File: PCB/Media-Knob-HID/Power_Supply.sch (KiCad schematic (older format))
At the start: 19 parts

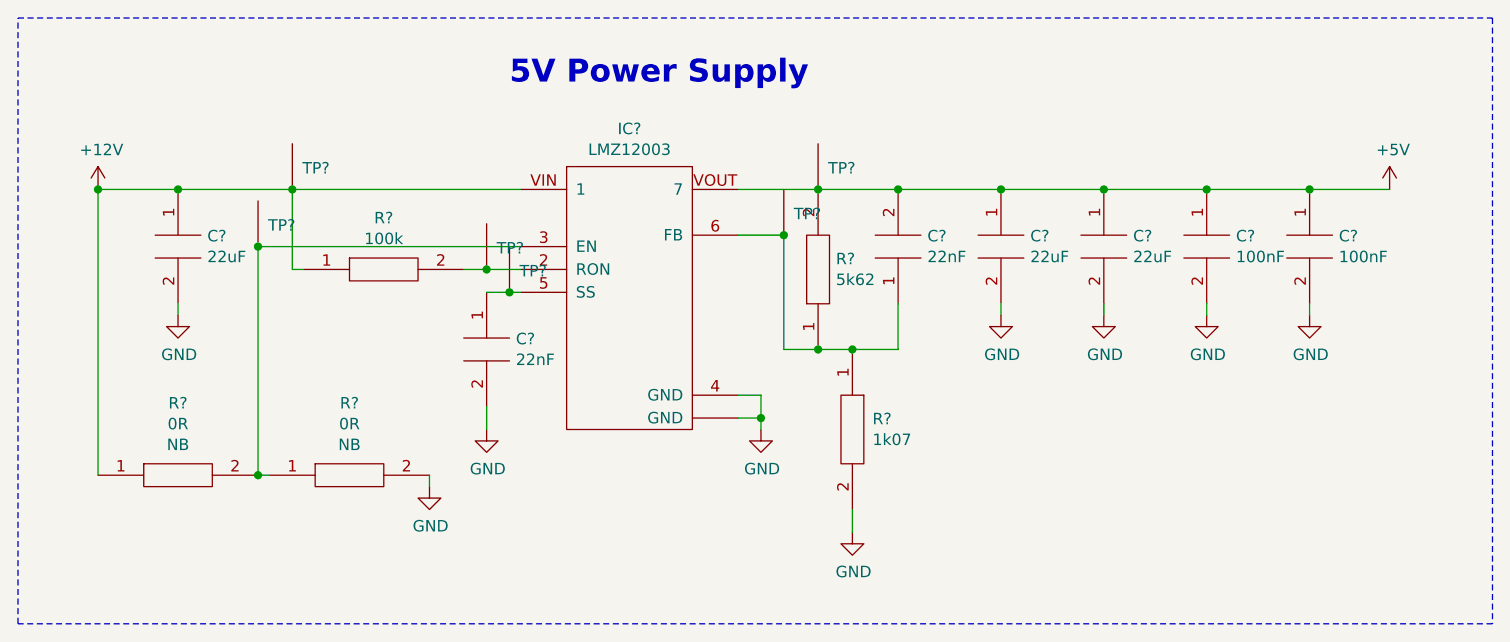
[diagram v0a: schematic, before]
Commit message: Port Switch für USB eingefügt
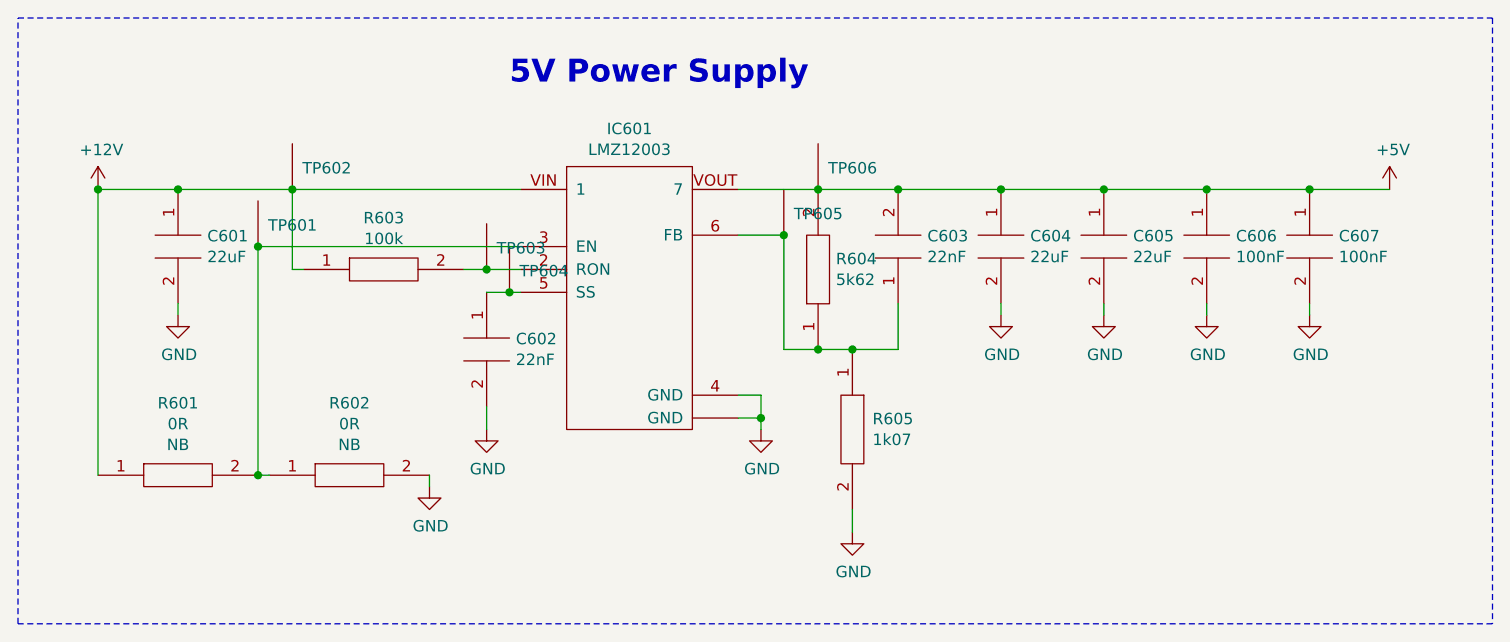
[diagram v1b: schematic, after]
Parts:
- gave numbers to parts that had none: 19
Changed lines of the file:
@@
 $Descr A3 16535 11693
 encoding utf-8
-Sheet 6 7
+Sheet 6 8
 Title "Media-Knob_HID"
 Date "2020-12-13"
@@
 $EndDescr
 $Comp
-L Artikel:LMZ12003 IC?
+L Artikel:LMZ12003 IC601
 U 1 1 607EAA9F
 P 3950 1900
-F 0 "IC?" H 3925 2615 50  0000 C CNN
+F 0 "IC601" H 3925 2615 50  0000 C CNN
 F 1 "LMZ12003" H 3925 2524 50  0000 C CNN
 F 2 "" H 3850 1850 50  0001 C CNN
@@
 $EndComp
 $Comp
-L power:GND #PWR?
+L power:GND #PWR0605
 U 1 1 607EB63F
 P 4500 2500
-F 0 "#PWR?" H 4500 2250 50  0001 C CNN
+F 0 "#PWR0605" H 4500 2250 50  0001 C CNN
 F 1 "GND" H 4505 2327 50  0000 C CNN
 F 2 "" H 4500 2500 50  0001 C CNN
@@
 Connection ~ 4500 2450
 $Comp
-L power:+12V #PWR?
+L power:+12V #PWR0601
 U 1 1 607EBAE6
 P 1600 1450
-F 0 "#PWR?" H 1600 1300 50  0001 C CNN
+F 0 "#PWR0601" H 1600 1300 50  0001 C CNN
 F 1 "+12V" H 1615 1623 50  0000 C CNN
 F 2 "" H 1600 1450 50  0001 C CNN
@@
 $EndComp
 $Comp
-L power:+5V #PWR?
+L power:+5V #PWR0611
 U 1 1 607ED18B
 P 7250 1450
-F 0 "#PWR?" H 7250 1300 50  0001 C CNN
+F 0 "#PWR0611" H 7250 1300 50  0001 C CNN
 F 1 "+5V" H 7265 1623 50  0000 C CNN
 F 2 "" H 7250 1450 50  0001 C CNN
@@
 $EndComp
 $Comp
-L Widerstand:5k62_0603 R?
+L Widerstand:5k62_0603 R604
 U 1 1 607EDDED
 P 4750 1800
-F 0 "R?" V 4796 1722 50  0000 R CNN
+F 0 "R604" V 4796 1722 50  0000 R CNN
 F 1 "5k62_0603" H 4600 1650 50  0001 L BNN
 F 2 "Widerstand:RESC1608" H 4800 1700 50  0001 L CNN
@@
 $EndComp
 $Comp
-L Widerstand:100K_0603 R?
+L Widerstand:100K_0603 R603
 U 1 1 607EE21B
 P 2850 1800
-F 0 "R?" H 2850 2025 50  0000 C CNN
+F 0 "R603" H 2850 2025 50  0000 C CNN
 F 1 "100K_0603" H 2700 1650 50  0001 L BNN
 F 2 "Widerstand:RESC1608" H 2900 1700 50  0001 L CNN
@@
 $EndComp
 $Comp
-L Widerstand:1K07_0603 R?
+L Widerstand:1K07_0603 R605
 U 1 1 607EE8B5
 P 4900 2500
-F 0 "R?" V 4854 2588 50  0000 L CNN
+F 0 "R605" V 4854 2588 50  0000 L CNN
 F 1 "1K07_0603" H 4750 2350 50  0001 L BNN
 F 2 "Widerstand:RESC1608" H 4950 2400 50  0001 L CNN
@@
 	2450 1800 2500 1800
 $Comp
-L power:GND #PWR?
+L power:GND #PWR0606
 U 1 1 607F0657
 P 4900 2950
-F 0 "#PWR?" H 4900 2700 50  0001 C CNN
+F 0 "#PWR0606" H 4900 2700 50  0001 C CNN
 F 1 "GND" H 4905 2777 50  0000 C CNN
 F 2 "" H 4900 2950 50  0001 C CNN
@@
 $EndComp
 $Comp
-L Kondensator:22u_1210 C?
+L Kondensator:22u_1210 C604
 U 1 1 607F14FE
 P 5550 1700
-F 0 "C?" V 5504 1828 50  0000 L CNN
+F 0 "C604" V 5504 1828 50  0000 L CNN
 F 1 "22u_1210" H 5550 1550 50  0001 L CNN
 F 2 "Kondensator:CAPC3225" H 5550 1550 50  0001 L CNN
@@
 $EndComp
 $Comp
-L Kondensator:22u_1210 C?
+L Kondensator:22u_1210 C605
 U 1 1 607F1CDA
 P 6000 1700
-F 0 "C?" V 5954 1828 50  0000 L CNN
+F 0 "C605" V 5954 1828 50  0000 L CNN
 F 1 "22u_1210" H 6000 1550 50  0001 L CNN
 F 2 "Kondensator:CAPC3225" H 6000 1550 50  0001 L CNN
@@
 $EndComp
 $Comp
-L Kondensator:100n_0603 C?
+L Kondensator:100n_0603 C606
 U 1 1 607F23BF
 P 6450 1700
-F 0 "C?" V 6404 1828 50  0000 L CNN
+F 0 "C606" V 6404 1828 50  0000 L CNN
 F 1 "100n_0603" H 6450 1550 50  0001 L CNN
 F 2 "Kondensator:CAPC1608" H 6450 1550 50  0001 L CNN
@@
 $EndComp
 $Comp
-L Kondensator:100n_0603 C?
+L Kondensator:100n_0603 C607
 U 1 1 607F2D3B
 P 6900 1700
-F 0 "C?" V 6854 1828 50  0000 L CNN
+F 0 "C607" V 6854 1828 50  0000 L CNN
 F 1 "100n_0603" H 6900 1550 50  0001 L CNN
 F 2 "Kondensator:CAPC1608" H 6900 1550 50  0001 L CNN
@@
 $EndComp
 $Comp
-L Kondensator:22n_0603 C?
+L Kondensator:22n_0603 C602
 U 1 1 607F35FE
 P 3300 2150
-F 0 "C?" V 3254 2278 50  0000 L CNN
+F 0 "C602" V 3254 2278 50  0000 L CNN
 F 1 "22n_0603" H 3300 2000 50  0001 L CNN
 F 2 "Kondensator:CAPC1608" H 3300 2000 50  0001 L CNN
@@
 $EndComp
 $Comp
-L Kondensator:22n_0603 C?
+L Kondensator:22n_0603 C603
 U 1 1 607F42DB
 P 5100 1700
-F 0 "C?" V 5146 1572 50  0000 R CNN
+F 0 "C603" V 5146 1572 50  0000 R CNN
 F 1 "22n_0603" H 5100 1550 50  0001 L CNN
 F 2 "Kondensator:CAPC1608" H 5100 1550 50  0001 L CNN
@@
 	3300 1900 3400 1900
 $Comp
-L power:GND #PWR?
+L power:GND #PWR0604
 U 1 1 607F4AD1
 P 3300 2500
-F 0 "#PWR?" H 3300 2250 50  0001 C CNN
+F 0 "#PWR0604" H 3300 2250 50  0001 C CNN
 F 1 "GND" H 3305 2327 50  0000 C CNN
 F 2 "" H 3300 2500 50  0001 C CNN
@@
 Connection ~ 4750 2150
 $Comp
-L Kondensator:22u_1210 C?
+L Kondensator:22u_1210 C601
 U 1 1 607F930C
 P 1950 1700
-F 0 "C?" V 1904 1828 50  0000 L CNN
+F 0 "C601" V 1904 1828 50  0000 L CNN
 F 1 "22u_1210" H 1950 1550 50  0001 L CNN
 F 2 "Kondensator:CAPC3225" H 1950 1550 50  0001 L CNN
@@
 	1950 1450 2450 1450
 $Comp
-L power:GND #PWR?
+L power:GND #PWR0602
 U 1 1 607FA0A7
 P 1950 2000
-F 0 "#PWR?" H 1950 1750 50  0001 C CNN
+F 0 "#PWR0602" H 1950 1750 50  0001 C CNN
 F 1 "GND" H 1955 1827 50  0000 C CNN
 F 2 "" H 1950 2000 50  0001 C CNN
@@
 	6900 1450 7250 1450
 $Comp
-L power:GND #PWR?
+L power:GND #PWR0607
 U 1 1 607FC441
 P 5550 2000
-F 0 "#PWR?" H 5550 1750 50  0001 C CNN
+F 0 "#PWR0607" H 5550 1750 50  0001 C CNN
 F 1 "GND" H 5555 1827 50  0000 C CNN
 F 2 "" H 5550 2000 50  0001 C CNN
@@
 $EndComp
 $Comp
-L power:GND #PWR?
+L power:GND #PWR0608
 U 1 1 607FC82F
 P 6000 2000
-F 0 "#PWR?" H 6000 1750 50  0001 C CNN
+F 0 "#PWR0608" H 6000 1750 50  0001 C CNN
 F 1 "GND" H 6005 1827 50  0000 C CNN
 F 2 "" H 6000 2000 50  0001 C CNN
@@
 $EndComp
 $Comp
-L power:GND #PWR?
+L power:GND #PWR0609
 U 1 1 607FCA1D
 P 6450 2000
-F 0 "#PWR?" H 6450 1750 50  0001 C CNN
+F 0 "#PWR0609" H 6450 1750 50  0001 C CNN
 F 1 "GND" H 6455 1827 50  0000 C CNN
 F 2 "" H 6450 2000 50  0001 C CNN
@@
 $EndComp
 $Comp
-L power:GND #PWR?
+L power:GND #PWR0610
 U 1 1 607FCBF0
 P 6900 2000
-F 0 "#PWR?" H 6900 1750 50  0001 C CNN
+F 0 "#PWR0610" H 6900 1750 50  0001 C CNN
 F 1 "GND" H 6905 1827 50  0000 C CNN
 F 2 "" H 6900 2000 50  0001 C CNN
@@
 	6900 2000 6900 1950
 $Comp
-L Widerstand:0R_0603 R?
+L Widerstand:0R_0603 R601
 U 1 1 607FE1D2
 P 1950 2700
-F 0 "R?" H 1950 3015 50  0000 C CNN
+F 0 "R601" H 1950 3015 50  0000 C CNN
 F 1 "0R_0603" H 1800 2550 50  0001 L BNN
 F 2 "Widerstand:RESC1608" H 1350 2900 50  0001 L CNN
@@
 $EndComp
 $Comp
-L Widerstand:0R_0603 R?
+L Widerstand:0R_0603 R602
 U 1 1 607FE5D5
 P 2700 2700
-F 0 "R?" H 2700 3015 50  0000 C CNN
+F 0 "R602" H 2700 3015 50  0000 C CNN
 F 1 "0R_0603" H 2550 2550 50  0001 L BNN
 F 2 "Widerstand:RESC1608" H 2100 2900 50  0001 L CNN
@@
 Connection ~ 2300 2700
 $Comp
-L power:GND #PWR?
+L power:GND #PWR0603
 U 1 1 608019ED
 P 3050 2750
-F 0 "#PWR?" H 3050 2500 50  0001 C CNN
+F 0 "#PWR0603" H 3050 2500 50  0001 C CNN
 F 1 "GND" H 3055 2577 50  0000 C CNN
 F 2 "" H 3050 2750 50  0001 C CNN
@@
 	3050 2750 3050 2700
 $Comp
-L Technik:TP_100 TP?
+L Technik:TP_100 TP606
 U 1 1 60802711
 P 4750 1450
-F 0 "TP?" H 4794 1543 50  0000 L CNN
+F 0 "TP606" H 4794 1543 50  0000 L CNN
 F 1 "TP_100" H 4800 1500 50  0001 L CNN
 F 2 "Technik:TP100;" H 4750 1450 50  0001 C CNN
@@
 $EndComp
 $Comp
-L Technik:TP_100 TP?
+L Technik:TP_100 TP602
 U 1 1 60802A68
 P 2450 1450
-F 0 "TP?" H 2494 1543 50  0000 L CNN
+F 0 "TP602" H 2494 1543 50  0000 L CNN
 F 1 "TP_100" H 2500 1500 50  0001 L CNN
 F 2 "Technik:TP100;" H 2450 1450 50  0001 C CNN
@@
 $EndComp
 $Comp
-L Technik:TP_100 TP?
+L Technik:TP_100 TP601
 U 1 1 60802E07
 P 2300 1700
-F 0 "TP?" H 2344 1793 50  0000 L CNN
+F 0 "TP601" H 2344 1793 50  0000 L CNN
 F 1 "TP_100" H 2350 1750 50  0001 L CNN
 F 2 "Technik:TP100;" H 2300 1700 50  0001 C CNN
@@
 Connection ~ 2300 1700
 $Comp
-L Technik:TP_100 TP?
+L Technik:TP_100 TP603
 U 1 1 60802FED
 P 3300 1800
-F 0 "TP?" H 3344 1893 50  0000 L CNN
+F 0 "TP603" H 3344 1893 50  0000 L CNN
 F 1 "TP_100" H 3350 1850 50  0001 L CNN
 F 2 "Technik:TP100;" H 3300 1800 50  0001 C CNN
@@
 	3300 1800 3450 1800
 $Comp
-L Technik:TP_100 TP?
+L Technik:TP_100 TP604
 U 1 1 60803291
 P 3400 1900
-F 0 "TP?" H 3444 1993 50  0000 L CNN
+F 0 "TP604" H 3444 1993 50  0000 L CNN
 F 1 "TP_100" H 3450 1950 50  0001 L CNN
 F 2 "Technik:TP100;" H 3400 1900 50  0001 C CNN
@@
 	3400 1900 3450 1900
 $Comp
-L Technik:TP_100 TP?
+L Technik:TP_100 TP605
 U 1 1 60803468
 P 4600 1650
-F 0 "TP?" H 4644 1743 50  0000 L CNN
+F 0 "TP605" H 4644 1743 50  0000 L CNN
 F 1 "TP_100" H 4650 1700 50  0001 L CNN
 F 2 "Technik:TP100;" H 4600 1650 50  0001 C CNN
